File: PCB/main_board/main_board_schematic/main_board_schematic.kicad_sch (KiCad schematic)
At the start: 4 parts

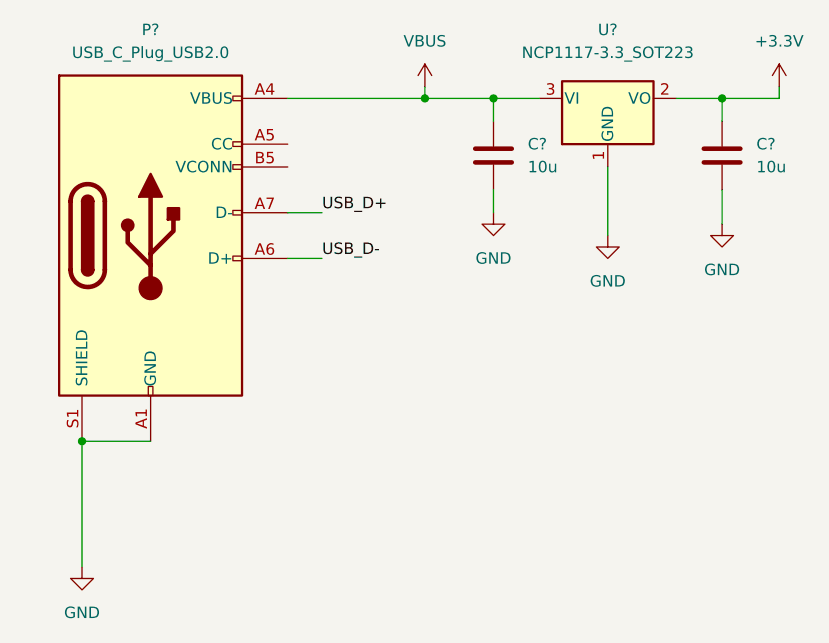
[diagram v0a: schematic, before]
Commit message: Added pull downs for cc and vconn
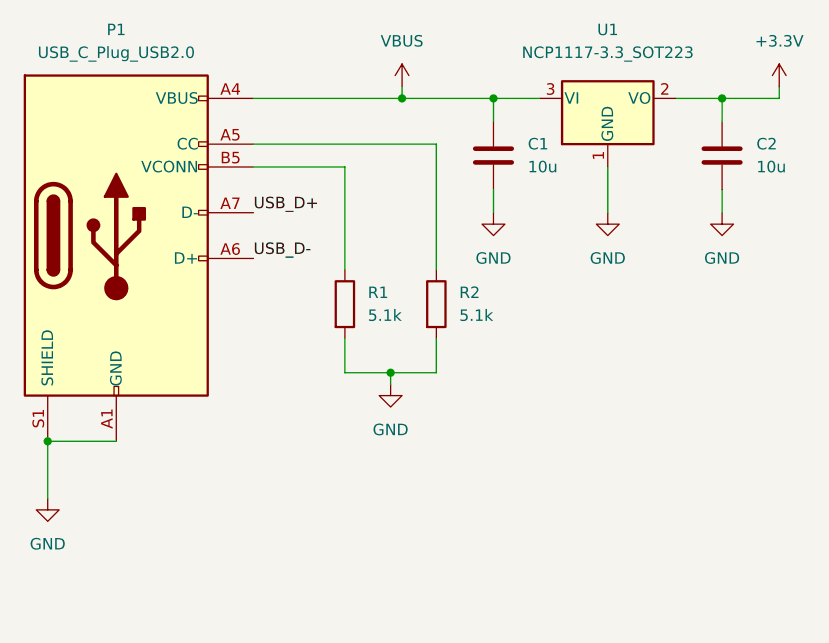
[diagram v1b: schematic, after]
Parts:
- added R1, R2: 5.1k, symbol Device:R
- gave numbers to parts that had none: 4
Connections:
- net GND: now also R1.2, R2.2
- net at P1.A5 (CC): now also R2.1
- net at P1.B5 (VCONN): now also R1.1
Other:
- moved on the sheet: P1

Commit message: Fixed wiring mistake...
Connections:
- net USB_D+: now also P1.A6 (D+); no longer P1.A7 (D-)
- net USB_D-: now also P1.A7 (D-); no longer P1.A6 (D+)
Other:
- moved on the sheet: C1, C2, R1, R2, U1

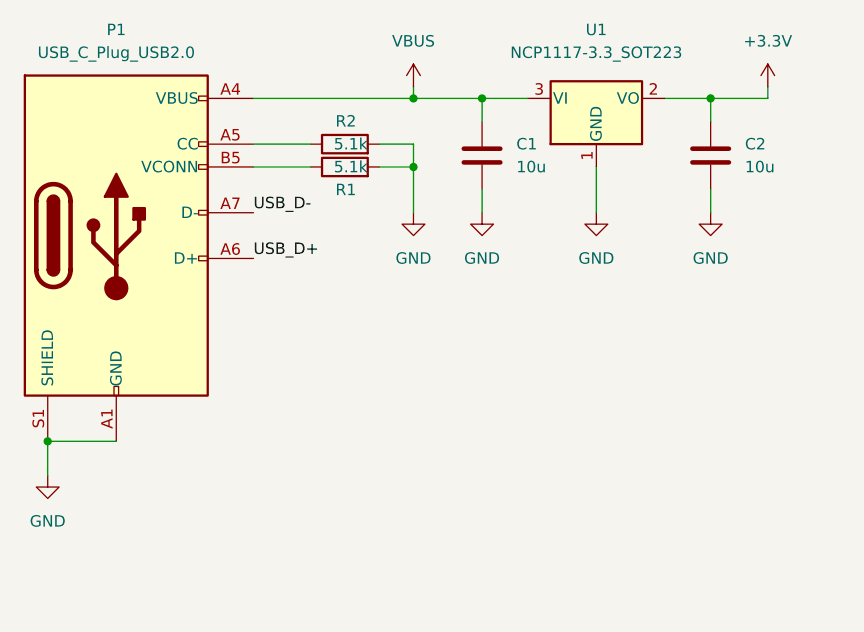
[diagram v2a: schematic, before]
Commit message: Added label for power supply and usb
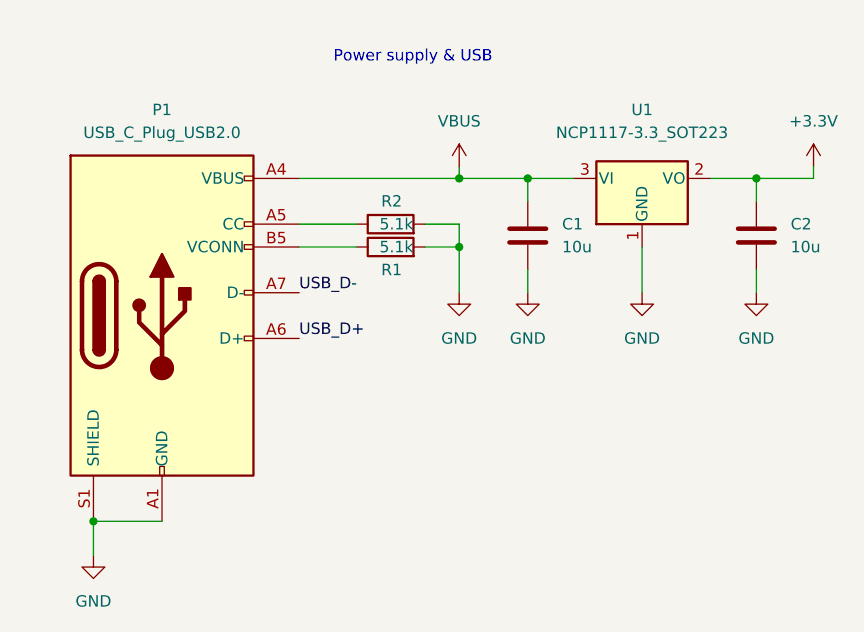
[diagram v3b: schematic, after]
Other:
- note added: "Power supply & USB"
- moved on the sheet: C1, C2, P1, R1, R2, U1

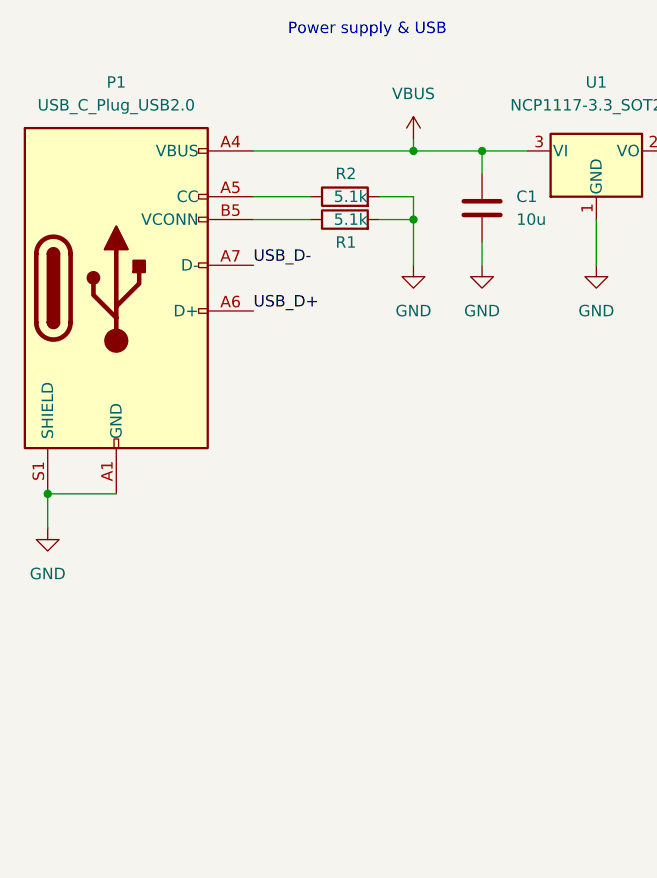
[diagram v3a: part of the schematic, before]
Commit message: Created the crystal oscilator
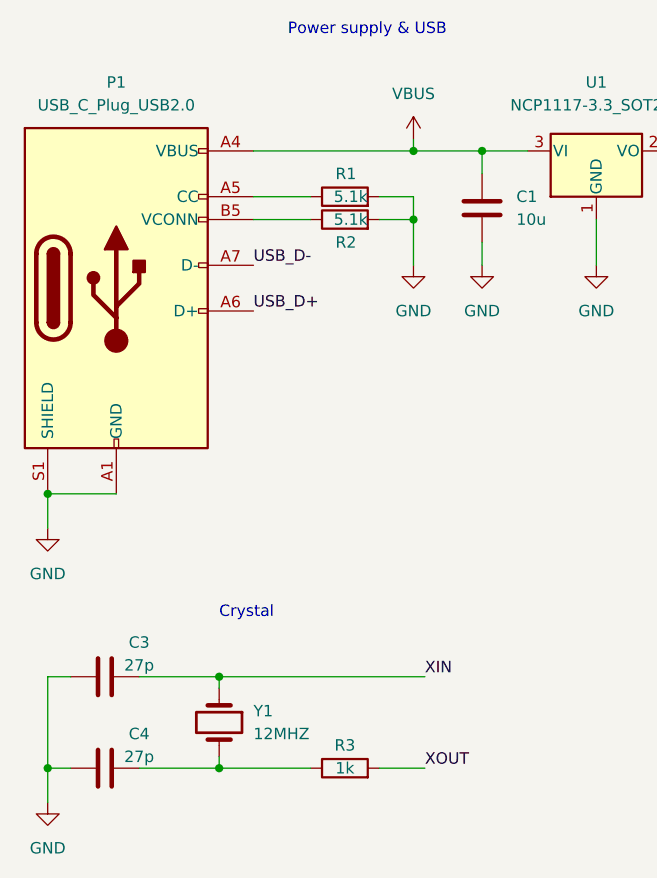
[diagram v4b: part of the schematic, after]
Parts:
- added C3, C4: 27p, symbol Device:C
- added R3: 1k, symbol Device:R
- added Y1: 12MHZ, symbol Device:Crystal
- renumbered R2 to R1, R1 to R2
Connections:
- net GND: now also C3.2, C4.1
- new net: C4.2, R3.1, Y1.2
- new net XIN: C3.1, Y1.1
- new net XOUT: R3.2
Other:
- note added: "Crystal"

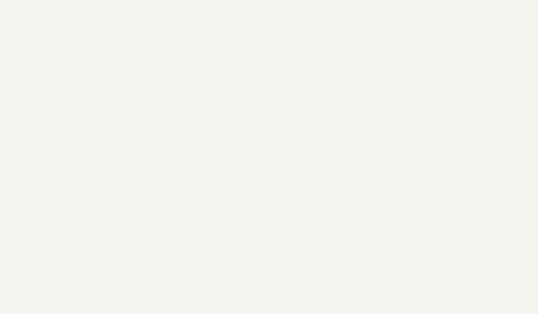
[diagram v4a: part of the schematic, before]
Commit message: Project organisation - added photos of circuit sections and a title
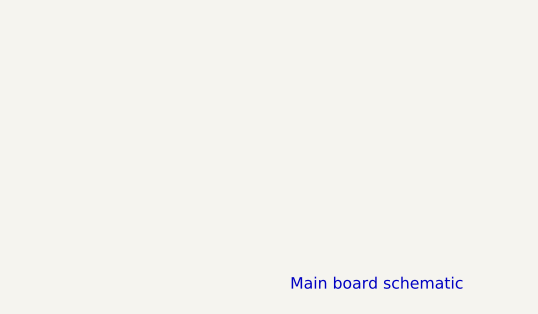
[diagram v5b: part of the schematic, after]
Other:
- note added: "Main board schematic"
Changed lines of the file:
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@@
+    (effects (font (size 1.27 1.27)) (justify left bottom))
+  )
+  (text "Main board schematic\n" (at 186.69 190.5 0)
     (effects (font (size 1.27 1.27)) (justify left bottom))
   )

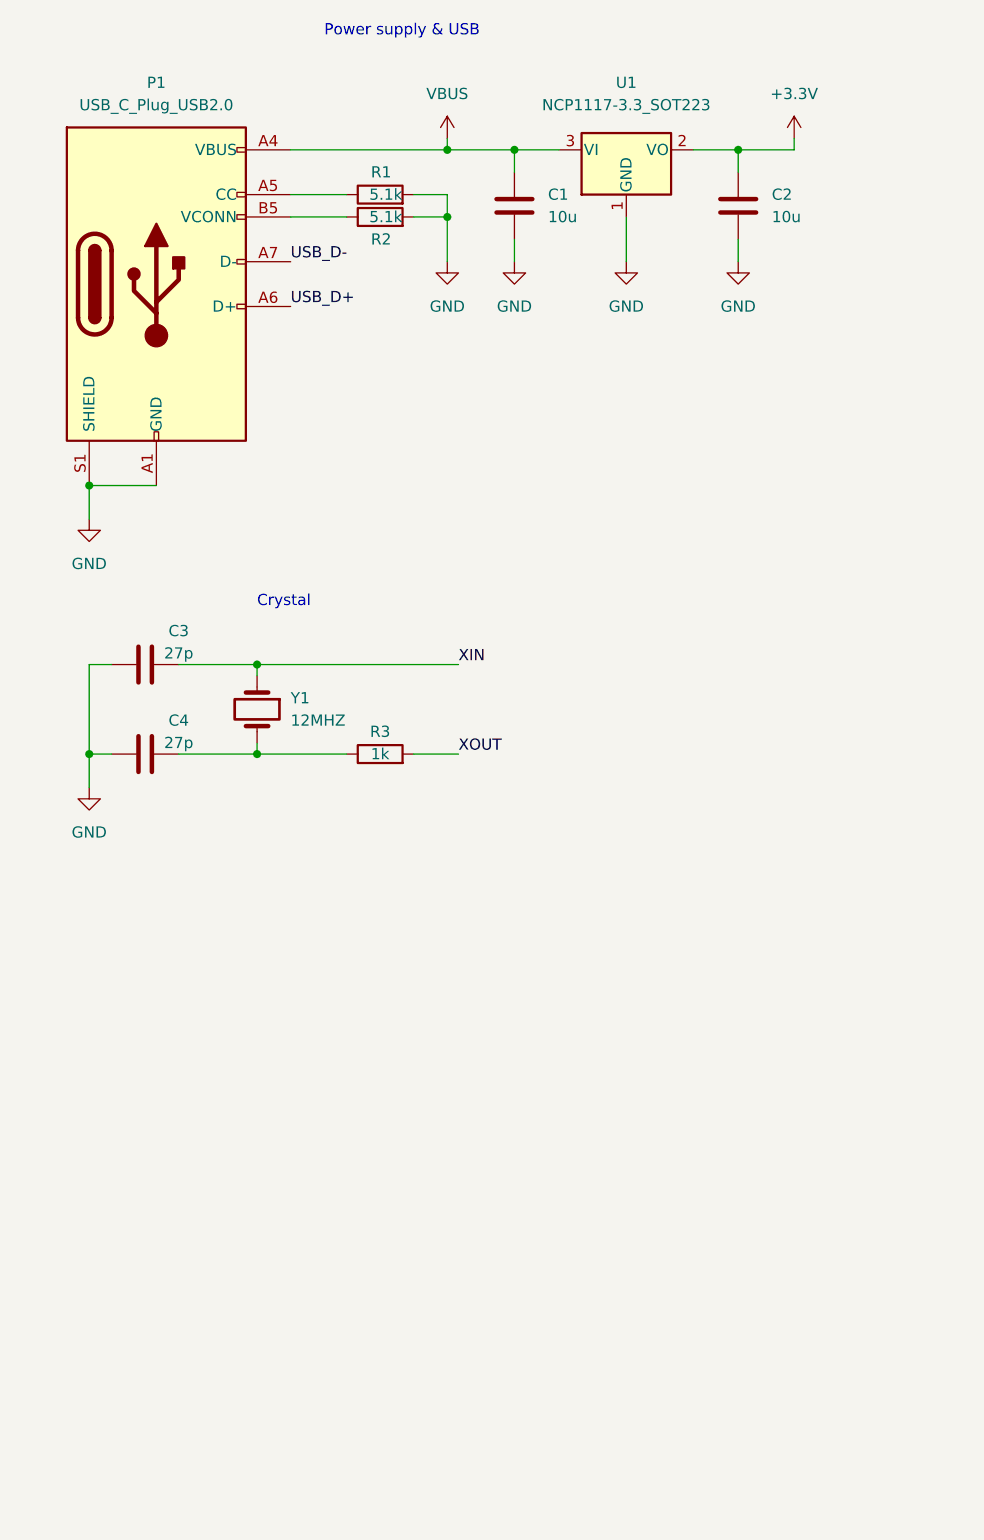
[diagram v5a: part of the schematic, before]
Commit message: Created a schematic for the flash storage
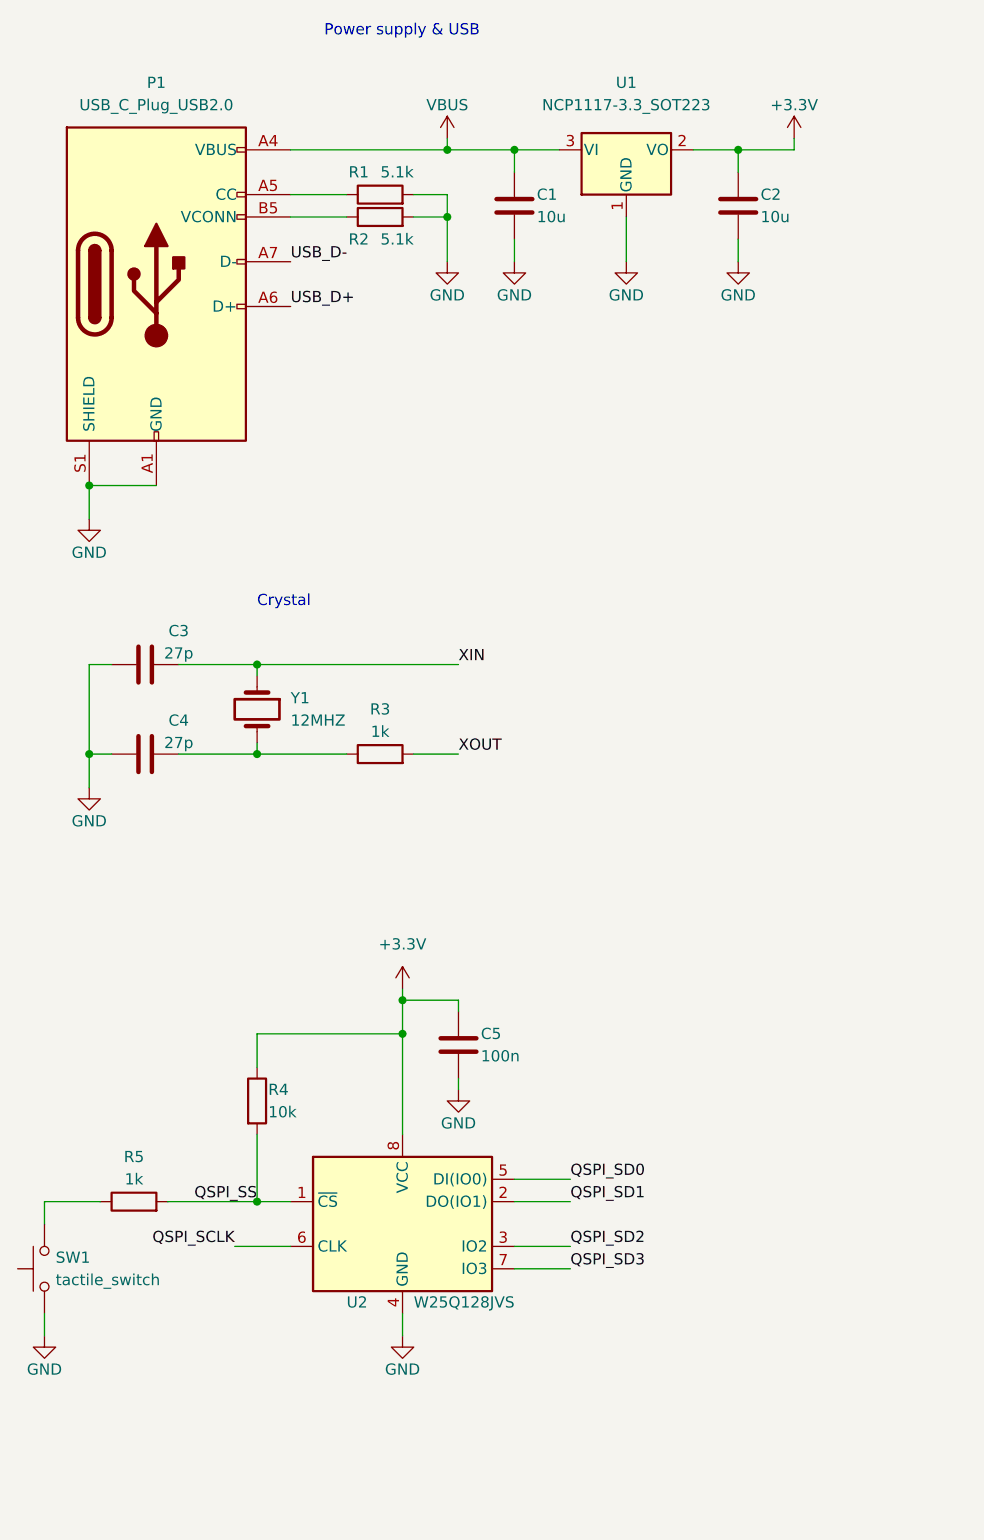
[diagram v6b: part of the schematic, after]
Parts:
- added C5: 100n, symbol Device:C
- added R4: 10k, symbol Device:R
- added R5: 1k, symbol Device:R
- added SW1: tactile_switch, symbol Switch:SW_MEC_5G
- added U2: W25Q128JVS, Package_SO:SOIC-8_5.23x5.23mm_P1.27mm, symbol Memory_Flash:W25Q128JVS
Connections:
- net +3.3V: now also C5.1, R4.1, U2.8 (VCC)
- net GND: now also C5.2, SW1.1 (A), SW1.2 (A), U2.4 (GND)
- new net: R5.1, SW1.3 (B), SW1.4 (B)
- new net QSPI_SCLK: U2.6 (CLK)
- new net QSPI_SD0: U2.5 (DI(IO0))
- new net QSPI_SD1: U2.2 (DO(IO1))
- new net QSPI_SD2: U2.3 (IO2)
- new net QSPI_SD3: U2.7 (IO3)
- new net QSPI_SS: R4.2, R5.2, U2.1 (~{CS})

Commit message: Moved the components around 'minor changes'
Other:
- note added: "Flash memory"
- moved on the sheet: C1, C2, C3, C4, C5, P1, R1, R2, R3, R4, R5, SW1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
